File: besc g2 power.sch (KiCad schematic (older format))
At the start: 169 parts, among them J1 PHASE WIRE, J2 PHASE WIRE, J3 PHASE WIRE, J4 BUSBAR, J5 BUSBAR, J6 IN+, J7 IN-, Q1 IRF135B203, Q10 IRF135B203, Q11 IRF135B203, Q12 IRF135B203, Q13 IRF135B203, Q14 IRF135B203, Q15 IRF135B203, Q16 IRF135B203, Q17 IRF135B203, Q18 IRF135B203, Q19 IRF135B203, Q2 IRF135B203, Q20 IRF135B203, Q21 IRF135B203, Q22 IRF135B203, Q23 IRF135B203, Q24 IRF135B203, Q3 IRF135B203, Q4 IRF135B203, Q5 IRF135B203, Q6 IRF135B203, Q7 IRF135B203, Q8 IRF135B203, Q9 IRF135B203, U1 UCC21520DW, U2 UCC21520DW, U3 UCC21520DW, U4 INA240A1D, U5 INA240A1D, U6 INA240A1D

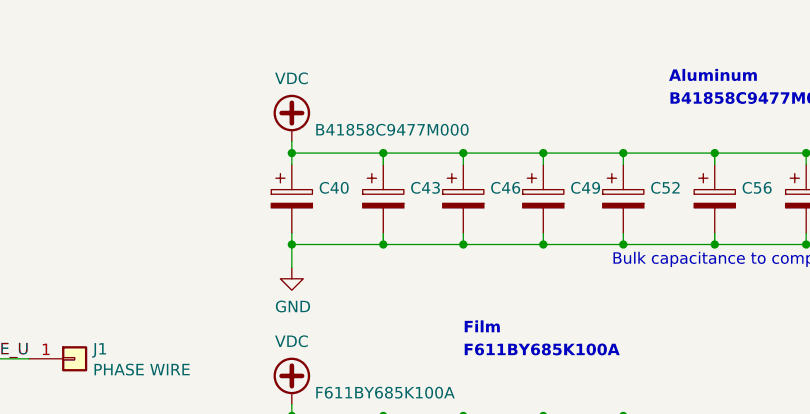
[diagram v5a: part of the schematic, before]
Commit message: replaced Al capacitors with shorter ones
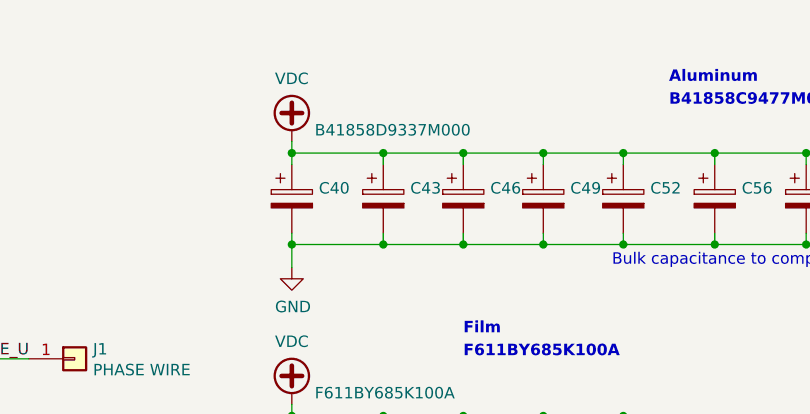
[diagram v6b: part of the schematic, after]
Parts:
- C40, C43, C46, C49, C52, C56, C57, C58, C59, C60, C61: value B41858C9477M000 -> B41858D9337M000; footprint Capacitor_THT:C_Radial_D18.0mm_H35.5mm_P7.50mm -> moje:C_Radial_D18.0mm_H25mm_P7.50mm
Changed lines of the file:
@@
 P 11850 1350
 F 0 "C40" H 11968 1396 50  0000 L CNN
-F 1 "B41858C9477M000" H 11950 1650 50  0000 L CNN
-F 2 "Capacitor_THT:C_Radial_D18.0mm_H35.5mm_P7.50mm" H 11888 1200 50  0001 C CNN
+F 1 "B41858D9337M000" H 11950 1650 50  0000 L CNN
+F 2 "moje:C_Radial_D18.0mm_H25mm_P7.50mm" H 11888 1200 50  0001 C CNN
 F 3 "~" H 11850 1350 50  0001 C CNN
 	1    11850 1350
@@
 P 12250 1350
 F 0 "C43" H 12368 1396 50  0000 L CNN
-F 1 "B41858C9477M000" H 12368 1305 50  0001 L CNN
-F 2 "Capacitor_THT:C_Radial_D18.0mm_H35.5mm_P7.50mm" H 12288 1200 50  0001 C CNN
+F 1 "B41858D9337M000" H 12368 1305 50  0001 L CNN
+F 2 "moje:C_Radial_D18.0mm_H25mm_P7.50mm" H 12288 1200 50  0001 C CNN
 F 3 "~" H 12250 1350 50  0001 C CNN
 	1    12250 1350
@@
 P 12600 1350
 F 0 "C46" H 12718 1396 50  0000 L CNN
-F 1 "B41858C9477M000" H 12718 1305 50  0001 L CNN
-F 2 "Capacitor_THT:C_Radial_D18.0mm_H35.5mm_P7.50mm" H 12638 1200 50  0001 C CNN
+F 1 "B41858D9337M000" H 12718 1305 50  0001 L CNN
+F 2 "moje:C_Radial_D18.0mm_H25mm_P7.50mm" H 12638 1200 50  0001 C CNN
 F 3 "~" H 12600 1350 50  0001 C CNN
 	1    12600 1350
@@
 P 12950 1350
 F 0 "C49" H 13068 1396 50  0000 L CNN
-F 1 "B41858C9477M000" H 13068 1305 50  0001 L CNN
-F 2 "Capacitor_THT:C_Radial_D18.0mm_H35.5mm_P7.50mm" H 12988 1200 50  0001 C CNN
+F 1 "B41858D9337M000" H 13068 1305 50  0001 L CNN
+F 2 "moje:C_Radial_D18.0mm_H25mm_P7.50mm" H 12988 1200 50  0001 C CNN
 F 3 "~" H 12950 1350 50  0001 C CNN
 	1    12950 1350
@@
 P 13300 1350
 F 0 "C52" H 13418 1396 50  0000 L CNN
-F 1 "B41858C9477M000" H 13418 1305 50  0001 L CNN
-F 2 "Capacitor_THT:C_Radial_D18.0mm_H35.5mm_P7.50mm" H 13338 1200 50  0001 C CNN
+F 1 "B41858D9337M000" H 13418 1305 50  0001 L CNN
+F 2 "moje:C_Radial_D18.0mm_H25mm_P7.50mm" H 13338 1200 50  0001 C CNN
 F 3 "~" H 13300 1350 50  0001 C CNN
 	1    13300 1350
@@
 P 13700 1350
 F 0 "C56" H 13818 1396 50  0000 L CNN
-F 1 "B41858C9477M000" H 13818 1305 50  0001 L CNN
-F 2 "Capacitor_THT:C_Radial_D18.0mm_H35.5mm_P7.50mm" H 13738 1200 50  0001 C CNN
+F 1 "B41858D9337M000" H 13818 1305 50  0001 L CNN
+F 2 "moje:C_Radial_D18.0mm_H25mm_P7.50mm" H 13738 1200 50  0001 C CNN
 F 3 "~" H 13700 1350 50  0001 C CNN
 	1    13700 1350
@@
 P 14100 1350
 F 0 "C57" H 14218 1396 50  0000 L CNN
-F 1 "B41858C9477M000" H 14218 1305 50  0001 L CNN
-F 2 "Capacitor_THT:C_Radial_D18.0mm_H35.5mm_P7.50mm" H 14138 1200 50  0001 C CNN
+F 1 "B41858D9337M000" H 14218 1305 50  0001 L CNN
+F 2 "moje:C_Radial_D18.0mm_H25mm_P7.50mm" H 14138 1200 50  0001 C CNN
 F 3 "~" H 14100 1350 50  0001 C CNN
 	1    14100 1350
@@
 P 14500 1350
 F 0 "C58" H 14618 1396 50  0000 L CNN
-F 1 "B41858C9477M000" H 14618 1305 50  0001 L CNN
-F 2 "Capacitor_THT:C_Radial_D18.0mm_H35.5mm_P7.50mm" H 14538 1200 50  0001 C CNN
+F 1 "B41858D9337M000" H 14618 1305 50  0001 L CNN
+F 2 "moje:C_Radial_D18.0mm_H25mm_P7.50mm" H 14538 1200 50  0001 C CNN
 F 3 "~" H 14500 1350 50  0001 C CNN
 	1    14500 1350
@@
 P 14900 1350
 F 0 "C59" H 15018 1396 50  0000 L CNN
-F 1 "B41858C9477M000" H 15018 1305 50  0001 L CNN
-F 2 "Capacitor_THT:C_Radial_D18.0mm_H35.5mm_P7.50mm" H 14938 1200 50  0001 C CNN
+F 1 "B41858D9337M000" H 15018 1305 50  0001 L CNN
+F 2 "moje:C_Radial_D18.0mm_H25mm_P7.50mm" H 14938 1200 50  0001 C CNN
 F 3 "~" H 14900 1350 50  0001 C CNN
 	1    14900 1350
@@
 P 15250 1350
 F 0 "C60" H 15368 1396 50  0000 L CNN
-F 1 "B41858C9477M000" H 15368 1305 50  0001 L CNN
-F 2 "Capacitor_THT:C_Radial_D18.0mm_H35.5mm_P7.50mm" H 15288 1200 50  0001 C CNN
+F 1 "B41858D9337M000" H 15368 1305 50  0001 L CNN
+F 2 "moje:C_Radial_D18.0mm_H25mm_P7.50mm" H 15288 1200 50  0001 C CNN
 F 3 "~" H 15250 1350 50  0001 C CNN
 	1    15250 1350
@@
 P 15650 1350
 F 0 "C61" H 15768 1396 50  0000 L CNN
-F 1 "B41858C9477M000" H 15768 1305 50  0001 L CNN
-F 2 "Capacitor_THT:C_Radial_D18.0mm_H35.5mm_P7.50mm" H 15688 1200 50  0001 C CNN
+F 1 "B41858D9337M000" H 15768 1305 50  0001 L CNN
+F 2 "moje:C_Radial_D18.0mm_H25mm_P7.50mm" H 15688 1200 50  0001 C CNN
 F 3 "~" H 15650 1350 50  0001 C CNN
 	1    15650 1350
